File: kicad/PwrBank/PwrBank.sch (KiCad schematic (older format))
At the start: 2 parts

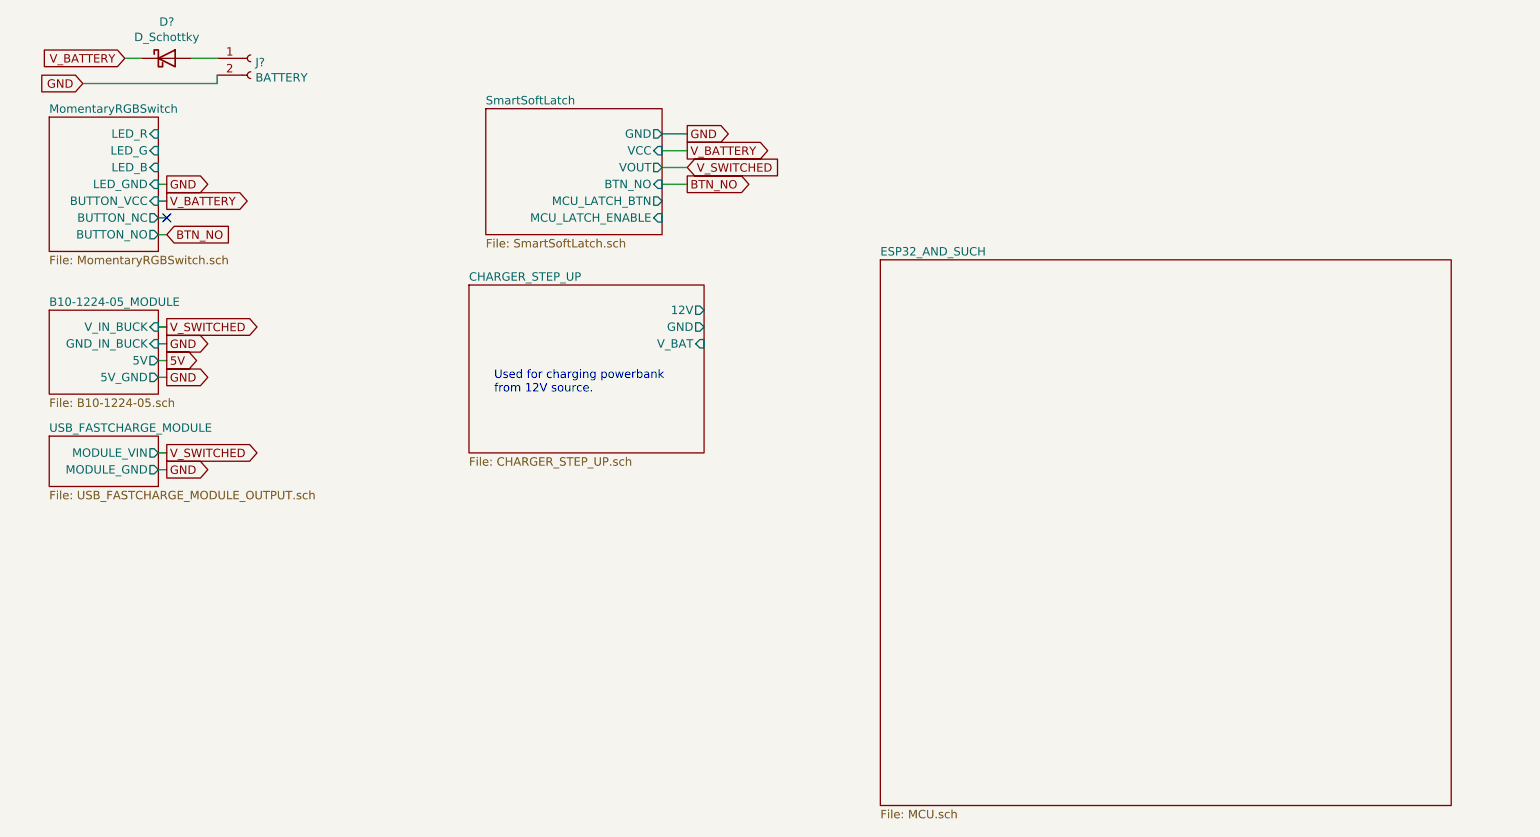
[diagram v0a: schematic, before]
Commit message: Working on/off system with safe shutdown and deepsleep inbetween
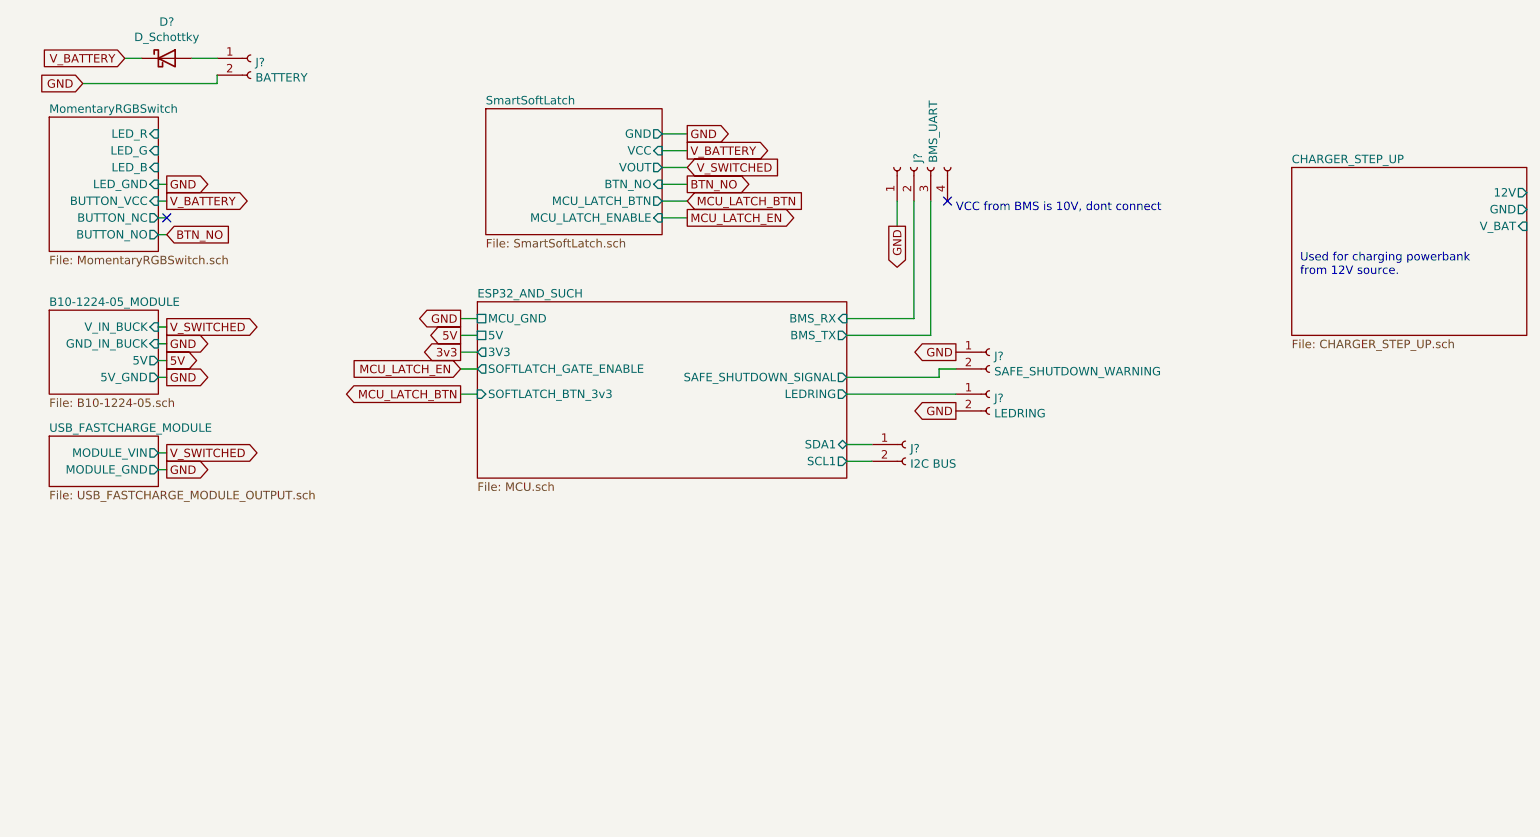
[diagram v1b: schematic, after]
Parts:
- added J?: I2C BUS, symbol Connector:Conn_01x02_Female
- added J?: LEDRING, symbol Connector:Conn_01x02_Female
- added J?: SAFE_SHUTDOWN_WARNING, symbol Connector:Conn_01x02_Female
- added J?: BMS_UART, symbol Connector:Conn_01x04_Female
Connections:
- net GND: now also J?.1 (Pin_1), J?.1 (Pin_1), J?.2 (Pin_2)
- new net ESP32_AND_SUCH/BMS_RX: J?.2 (Pin_2)
- new net ESP32_AND_SUCH/BMS_TX: J?.3 (Pin_3)
- new net ESP32_AND_SUCH/LEDRING: J?.1 (Pin_1)
- new net ESP32_AND_SUCH/SAFE_SHUTDOWN_SIGNAL: J?.2 (Pin_2)
- new net ESP32_AND_SUCH/SCL1: J?.2 (Pin_2)
- new net ESP32_AND_SUCH/SDA1: J?.1 (Pin_1)
- no-connect marks 1 -> 2
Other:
- note added: "VCC from BMS is 10V, dont connect\n\n"
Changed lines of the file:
@@
 $Descr A4 11693 8268
 encoding utf-8
-Sheet 1 8
+Sheet 1 9
 Title "Powerbank BMS Additional Circuitry"
 Date "2021-07-11"
@@
 	1350 3100 1300 3100
 $Sheet
-S 3150 2100 1400 1000
+S 8050 1400 1400 1000
 U 60F78247
 F0 "CHARGER_STEP_UP" 50
 F1 "CHARGER_STEP_UP.sch" 50
-F2 "12V" O R 4550 2250 50
-F3 "GND" O R 4550 2350 50
-F4 "V_BAT" I R 4550 2450 50
+F2 "12V" O R 9450 1550 50
+F3 "GND" O R 9450 1650 50
+F4 "V_BAT" I R 9450 1750 50
 $EndSheet
 $Comp
@@
 Wire Wire Line
 	850  900  1650 900
-Text Notes 3300 2750 0    50   ~ 0
+Text Notes 8100 2050 0    50   ~ 0
 Used for charging powerbank \nfrom 12V source.
 $Sheet
-S 5600 1950 3400 3250
+S 3200 2200 2200 1050
 U 60F2D9E7
 F0 "ESP32_AND_SUCH" 50
 F1 "MCU.sch" 50
-$EndSheet
+F2 "BMS_TX" O R 5400 2400 50
+F3 "BMS_RX" I R 5400 2300 50
+F4 "SAFE_SHUTDOWN_SIGNAL" O R 5400 2650 50
+F5 "SOFTLATCH_GATE_ENABLE" O L 3200 2600 50
+F6 "LEDRING" O R 5400 2750 50
+F7 "SDA1" B R 5400 3050 50
+F8 "SCL1" O R 5400 3150 50
+F9 "SOFTLATCH_BTN_3v3" I L 3200 2750 50
+F10 "5V" U L 3200 2400 50
+F11 "3V3" O L 3200 2500 50
+F12 "MCU_GND" U L 3200 2300 50
+$EndSheet
+Wire Wire Line
+	3100 2400 3200 2400
+Text GLabel 3100 2400 0    50   Output ~ 0
+5V
+Text GLabel 3100 2300 0    50   Output ~ 0
+GND
+Wire Wire Line
+	3100 2300 3200 2300
+Text GLabel 3100 2500 0    50   Output ~ 0
+3v3
+Wire Wire Line
+	3100 2500 3200 2500
+Text GLabel 3100 2600 0    50   Input ~ 0
+MCU_LATCH_EN
+Wire Wire Line
+	3100 2600 3200 2600
+Text GLabel 4450 1700 2    50   Output ~ 0
+MCU_LATCH_EN
+Wire Wire Line
+	4450 1700 4300 1700
+Text GLabel 3100 2750 0    50   Output ~ 0
+MCU_LATCH_BTN
+Wire Wire Line
+	3100 2750 3200 2750
+Wire Wire Line
+	4450 1600 4300 1600
+Text GLabel 4450 1600 2    50   Input ~ 0
+MCU_LATCH_BTN
+$Comp
+L Connector:Conn_01x02_Female J?
+U 1 1 60F61784
+P 5750 3050
+F 0 "J?" H 5778 3026 50  0000 L CNN
+F 1 "I2C BUS" H 5778 2935 50  0000 L CNN
+F 2 "" H 5750 3050 50  0001 C CNN
+F 3 "~" H 5750 3050 50  0001 C CNN
+	1    5750 3050
+	1    0    0    -1
+$EndComp
+Wire Wire Line
+	5400 3050 5550 3050
+Wire Wire Line
+	5550 3150 5400 3150
+$Comp
+L Connector:Conn_01x02_Female J?
+U 1 1 60F625B7
+P 6250 2750
+F 0 "J?" H 6278 2726 50  0000 L CNN
+F 1 "LEDRING" H 6278 2635 50  0000 L CNN
+F 2 "" H 6250 2750 50  0001 C CNN
+F 3 "~" H 6250 2750 50  0001 C CNN
+	1    6250 2750
+	1    0    0    -1
+$EndComp
+Wire Wire Line
+	5400 2750 6050 2750
+Text GLabel 6050 2850 0    50   Output ~ 0
+GND
+$Comp
+L Connector:Conn_01x02_Female J?
+U 1 1 60F64EEF
+P 6250 2500
+F 0 "J?" H 6278 2476 50  0000 L CNN
+F 1 "SAFE_SHUTDOWN_WARNING" H 6278 2385 50  0000 L CNN
+F 2 "" H 6250 2500 50  0001 C CNN
+F 3 "~" H 6250 2500 50  0001 C CNN
+	1    6250 2500
+	1    0    0    -1
+$EndComp
+Wire Wire Line
+	5400 2650 5950 2650
+Text GLabel 6050 2500 0    50   Output ~ 0
+GND
+Wire Wire Line
+	5950 2650 5950 2600
+Wire Wire Line
+	5950 2600 6050 2600
+$Comp
+L Connector:Conn_01x04_Female J?
+U 1 1 60F67167
+P 5800 1400
+F 0 "J?" H 5828 1376 50  0000 L CNN
+F 1 "BMS_UART" H 5828 1285 50  0000 L CNN
+F 2 "" H 5800 1400 50  0001 C CNN
+F 3 "~" H 5800 1400 50  0001 C CNN
+	1    5800 1400
+	0    -1   -1   0
+$EndComp
+Text GLabel 5700 1750 3    50   Output ~ 0
+GND
+Wire Wire Line
+	5400 2300 5800 2300
+Wire Wire Line
+	5800 2300 5800 1600
+Wire Wire Line
+	5900 1600 5900 2400
+Wire Wire Line
+	5900 2400 5400 2400
+Wire Wire Line
+	5700 1600 5700 1750
+NoConn ~ 6000 1600
+Text Notes 6050 1750 0    50   ~ 0
+VCC from BMS is 10V, dont connect\n\n
 $EndSCHEMATC

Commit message: UPDATE KICAD SOURCEFILES
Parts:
- removed D?: D_Schottky, symbol Device:D_Schottky
- removed J?: LEDRING, symbol Connector:Conn_01x02_Female
- removed J?: BATTERY, symbol Connector:Conn_01x02_Female
- added F1: 30A, Fuse:Fuseholder_Blade_Mini_Keystone_3568, symbol Device:Fuse_Small
- added J1: SCREW_TERMINALS_DCDC_MODULE, symbol Connector:Conn_01x04_Female
- added J2: CHARGEPORT, Connector_JST:JST_XH_B2B-XH-A_1x02_P2.50mm_Vertical, symbol Connector:Conn_01x02_Female
- J3, J5: renamed from J?; footprint (none) -> Connector_JST:JST_XH_B2B-XH-A_1x02_P2.50mm_Vertical
- J4: renamed from J?; footprint (none) -> Connector_JST:JST_XH_B4B-XH-A_1x04_P2.50mm_Vertical
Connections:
- net GND: now also J1.1 (Pin_1), J1.3 (Pin_3), J2.1 (Pin_1)
- new net +12V: J2.2 (Pin_2)
- new net +5V: J1.2 (Pin_2)
- new net +BATT: F1.2
- new net +BATT_SWITCHED: J1.4 (Pin_4)
- new net V_BATTERY_CHARGING: F1.1
- no-connect marks 2 -> 4
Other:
- note added: "BMS Battery in port and charging port."

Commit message: Kicad files update
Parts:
- removed J3: I2C BUS, Connector_JST:JST_XH_B2B-XH-A_1x02_P2.50mm_Vertical, symbol Connector:Conn_01x02_Female
- added J5: OLED_CONN, Connector_JST:JST_XH_B4B-XH-A_1x04_P2.50mm_Vertical, symbol Connector:Conn_01x04_Female
- renumbered J4 to J3, J5 to J4
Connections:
- net GND: now also J5.4 (Pin_4)
- new net +3V3: J5.3 (Pin_3)
- new net ESP32_AND_SUCH/SCL2: J5.2 (Pin_2)
- new net ESP32_AND_SUCH/SDA2: J5.1 (Pin_1)
- no-connect marks 4 -> 2
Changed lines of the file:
@@
 $Descr A4 11693 8268
 encoding utf-8
-Sheet 1 8
+Sheet 1 9
 Title "Powerbank BMS Additional Circuitry"
 Date "2021-07-11"
@@
 F3 "LED_G" I R 1250 900 50
 F4 "LED_B" I R 1250 1000 50
-F7 "BUTTON_NC" O R 1250 1100 50
-F8 "BUTTON_NO" O R 1250 1200 50
+F5 "BUTTON_NC" O R 1250 1100 50
+F6 "BUTTON_NO" O R 1250 1200 50
 $EndSheet
 NoConn ~ 1250 1100
@@
 F0 "SmartSoftLatch" 50
 F1 "SmartSoftLatch.sch" 50
-F3 "BTN_NO" I R 4300 1500 50
-F5 "MCU_LATCH_BTN" O R 4300 1600 50
-F6 "MCU_LATCH_ENABLE" I R 4300 1700 50
+F2 "BTN_NO" I R 4300 1500 50
+F3 "MCU_LATCH_BTN" O R 4300 1600 50
+F4 "MCU_LATCH_ENABLE" I R 4300 1700 50
 $EndSheet
 Text GLabel 4450 1500 2    50   Output ~ 0
@@
 F0 "CHARGER_STEP_UP" 50
 F1 "CHARGER_STEP_UP.sch" 50
-F3 "V_BATTERY_CHARGING" O R 4600 4000 50
+F2 "V_BATTERY_CHARGING" O R 4600 4000 50
 $EndSheet
 Text Notes 3250 4300 0    50   ~ 0
@@
 F4 "SAFE_SHUTDOWN_SIGNAL" O R 5400 2650 50
 F5 "SOFTLATCH_GATE_ENABLE" O L 3200 2600 50
-F6 "LEDRING" O R 5400 2750 50
-F7 "SDA1" B R 5400 3050 50
-F8 "SCL1" O R 5400 3150 50
-F9 "SOFTLATCH_BTN_3v3" I L 3200 2750 50
+F6 "SDA1" B R 5400 3050 50
+F7 "SCL1" O R 5400 3150 50
+F8 "SOFTLATCH_BTN_3v3" I L 3200 2750 50
+F9 "SCL2" O R 5400 2850 50
+F10 "SDA2" B R 5400 2750 50
 $EndSheet
 Text GLabel 3100 2600 0    50   Input ~ 0
@@
 Text GLabel 4450 1600 2    50   Input ~ 0
 MCU_LATCH_BTN
-$Comp
-L Connector:Conn_01x02_Female J3
-U 1 1 60F61784
-P 5750 3050
-F 0 "J3" H 5778 3026 50  0000 L CNN
-F 1 "I2C BUS" H 5778 2935 50  0000 L CNN
-F 2 "Connector_JST:JST_XH_B2B-XH-A_1x02_P2.50mm_Vertical" H 5750 3050 50  0001 C CNN
-F 3 "~" H 5750 3050 50  0001 C CNN
-	1    5750 3050
-	1    0    0    -1
-$EndComp
-Wire Wire Line
-	5400 3050 5550 3050
-Wire Wire Line
-	5550 3150 5400 3150
 Wire Wire Line
 	5400 2650 5950 2650
@@
 	5950 2600 6050 2600
 $Comp
-L Connector:Conn_01x04_Female J4
+L Connector:Conn_01x04_Female J3
 U 1 1 60F67167
 P 5800 1400
-F 0 "J4" V 5738 1112 50  0000 R CNN
+F 0 "J3" V 5738 1112 50  0000 R CNN
 F 1 "BMS_UART" V 5647 1112 50  0000 R CNN
 F 2 "Connector_JST:JST_XH_B4B-XH-A_1x04_P2.50mm_Vertical" H 5800 1400 50  0001 C CNN
@@
 Text Notes 600  3400 0    50   ~ 10
 BMS Battery in port and charging port.
-Text GLabel 5450 2750 2    50   Input ~ 0
-LEDRING_R
-Wire Wire Line
-	5450 2750 5400 2750
 Text GLabel 1300 800  2    50   Output ~ 0
 LEDRING_R
 Wire Wire Line
 	1300 800  1250 800
-NoConn ~ 1250 900
-NoConn ~ 1250 1000
 $Comp
 L power:+BATT #PWR03
@@
 $EndComp
 $Comp
-L Connector:Conn_01x02_Female J5
+L Connector:Conn_01x02_Female J4
 U 1 1 60F64EEF
 P 6250 2500
-F 0 "J5" H 6278 2476 50  0000 L CNN
+F 0 "J4" H 6278 2476 50  0000 L CNN
 F 1 "SAFE_SHUTDOWN_WARNING" H 6278 2385 50  0000 L CNN
 F 2 "Connector_JST:JST_XH_B2B-XH-A_1x02_P2.50mm_Vertical" H 6250 2500 50  0001 C CNN
@@
 	0    1    1    0
 $EndComp
+$Comp
+L Connector:Conn_01x04_Female J5
+U 1 1 60F9EBFE
+P 6350 2850
+F 0 "J5" H 6200 2400 50  0000 R CNN
+F 1 "OLED_CONN" H 6350 2550 50  0000 R CNN
+F 2 "Connector_JST:JST_XH_B4B-XH-A_1x04_P2.50mm_Vertical" H 6350 2850 50  0001 C CNN
+F 3 "https://www.jst-mfg.com/product/pdf/eng/eXH.pdf" H 6350 2850 50  0001 C CNN
+	1    6350 2850
+	1    0    0    -1
+$EndComp
+Wire Wire Line
+	5400 2750 6150 2750
+Wire Wire Line
+	5400 2850 6150 2850
+$Comp
+L power:+3.3V #PWR012
+U 1 1 60FA2045
+P 6150 2950
+F 0 "#PWR012" H 6150 2800 50  0001 C CNN
+F 1 "+3.3V" V 6165 3078 50  0000 L CNN
+F 2 "" H 6150 2950 50  0001 C CNN
+F 3 "" H 6150 2950 50  0001 C CNN
+	1    6150 2950
+	0    -1   -1   0
+$EndComp
+$Comp
+L power:GND #PWR013
+U 1 1 60FA2D4B
+P 6150 3050
+F 0 "#PWR013" H 6150 2800 50  0001 C CNN
+F 1 "GND" V 6155 2922 50  0000 R CNN
+F 2 "" H 6150 3050 50  0001 C CNN
+F 3 "" H 6150 3050 50  0001 C CNN
+	1    6150 3050
+	0    1    1    0
+$EndComp
+$Sheet
+S 6250 3600 1000 700
+U 60FA4163
+F0 "I2C_led_controller" 50
+F1 "I2CLEDCONTROL.sch" 50
+F2 "LEDRING_R" O L 6250 3700 50
+F3 "LEDRING_G" O L 6250 3800 50
+F4 "LEDRING_B" O L 6250 3900 50
+F5 "SDA" B L 6250 4100 50
+F6 "SCL" I L 6250 4200 50
+$EndSheet
+Wire Wire Line
+	5400 3150 5600 3150
+Wire Wire Line
+	5600 3150 5600 4200
+Wire Wire Line
+	5600 4200 6250 4200
+Wire Wire Line
+	5400 3050 5700 3050
+Wire Wire Line
+	5700 3050 5700 4100
+Wire Wire Line
+	5700 4100 6250 4100
+Text GLabel 6200 3700 0    50   Output ~ 0
+LEDRING_R
+Text GLabel 6200 3800 0    50   Output ~ 0
+LEDRING_G
+Text GLabel 6200 3900 0    50   Output ~ 0
+LEDRING_B
+Wire Wire Line
+	6200 3700 6250 3700
+Wire Wire Line
+	6200 3800 6250 3800
+Wire Wire Line
+	6200 3900 6250 3900
+Text GLabel 1300 900  2    50   Output ~ 0
+LEDRING_G
+Text GLabel 1300 1000 2    50   Output ~ 0
+LEDRING_B
+Wire Wire Line
+	1250 900  1300 900
+Wire Wire Line
+	1250 1000 1300 1000
 $EndSCHEMATC
